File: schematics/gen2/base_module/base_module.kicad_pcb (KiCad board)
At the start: 2 copper layers, 100 x 101.6 mm, 1 part

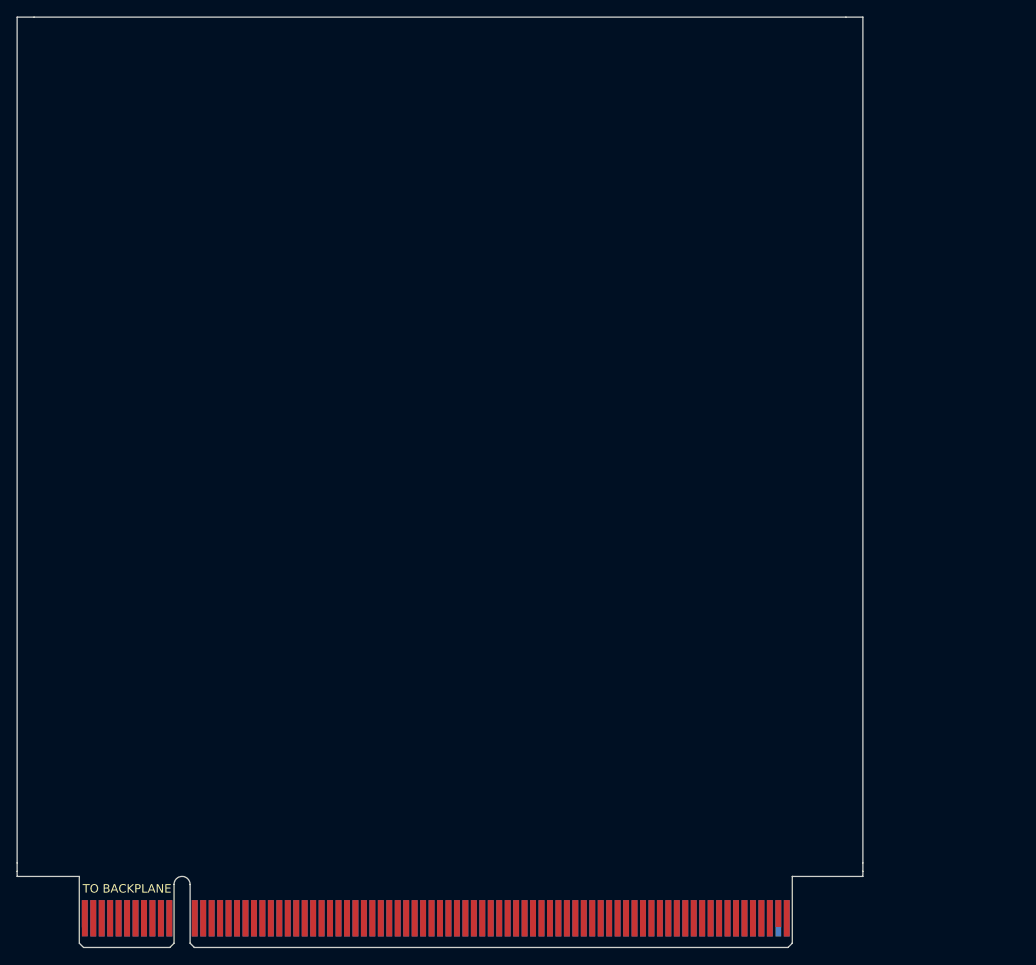
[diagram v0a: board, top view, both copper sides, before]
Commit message: fix: base module to match 100 mm x 100mm
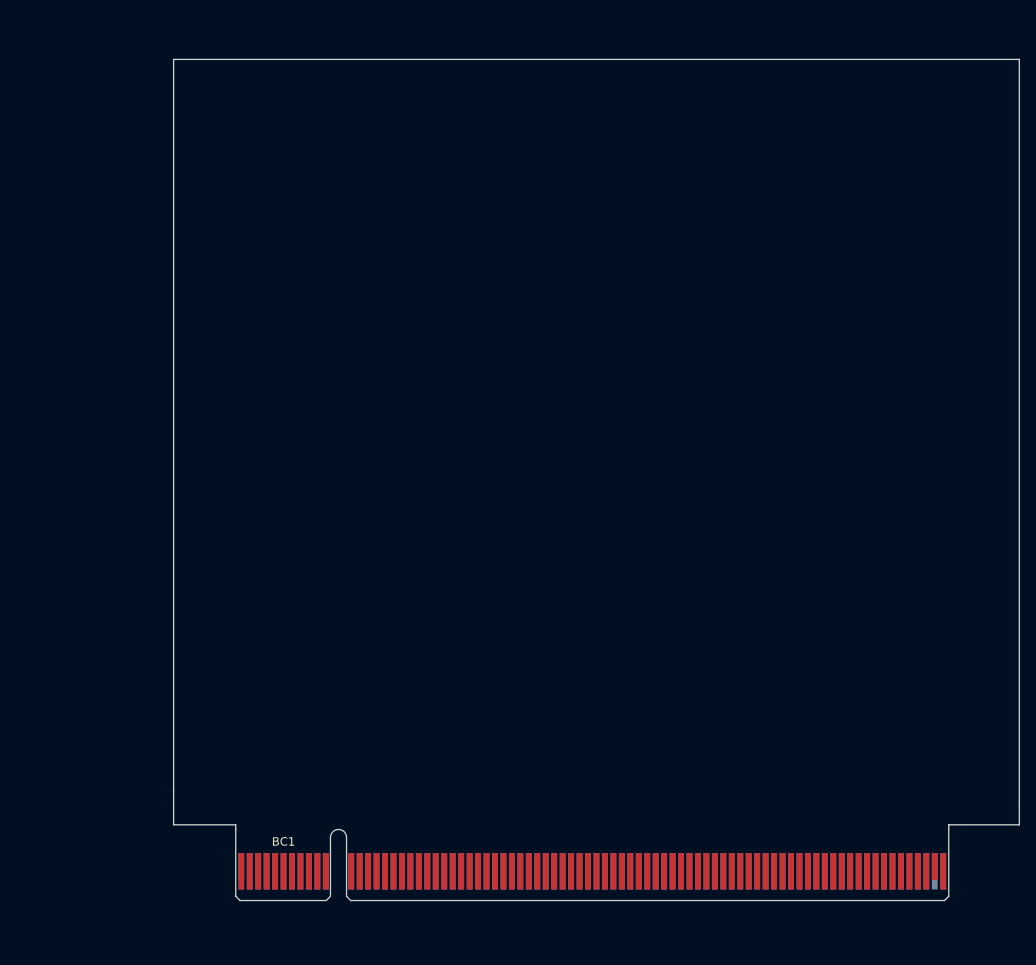
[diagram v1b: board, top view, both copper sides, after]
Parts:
- removed TO BACKPLANE: BusConnector, Connector_PCBEdge:BUS_PCIexpress_x16
- added BC1: BusConnector, Connector_PCBEdge:BUS_PCIexpress_x16, F.Cu at (96.5, 124.0)
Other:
- board size 100 x 101.6 mm -> 100 x 91 mm
